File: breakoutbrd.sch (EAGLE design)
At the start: 6 parts

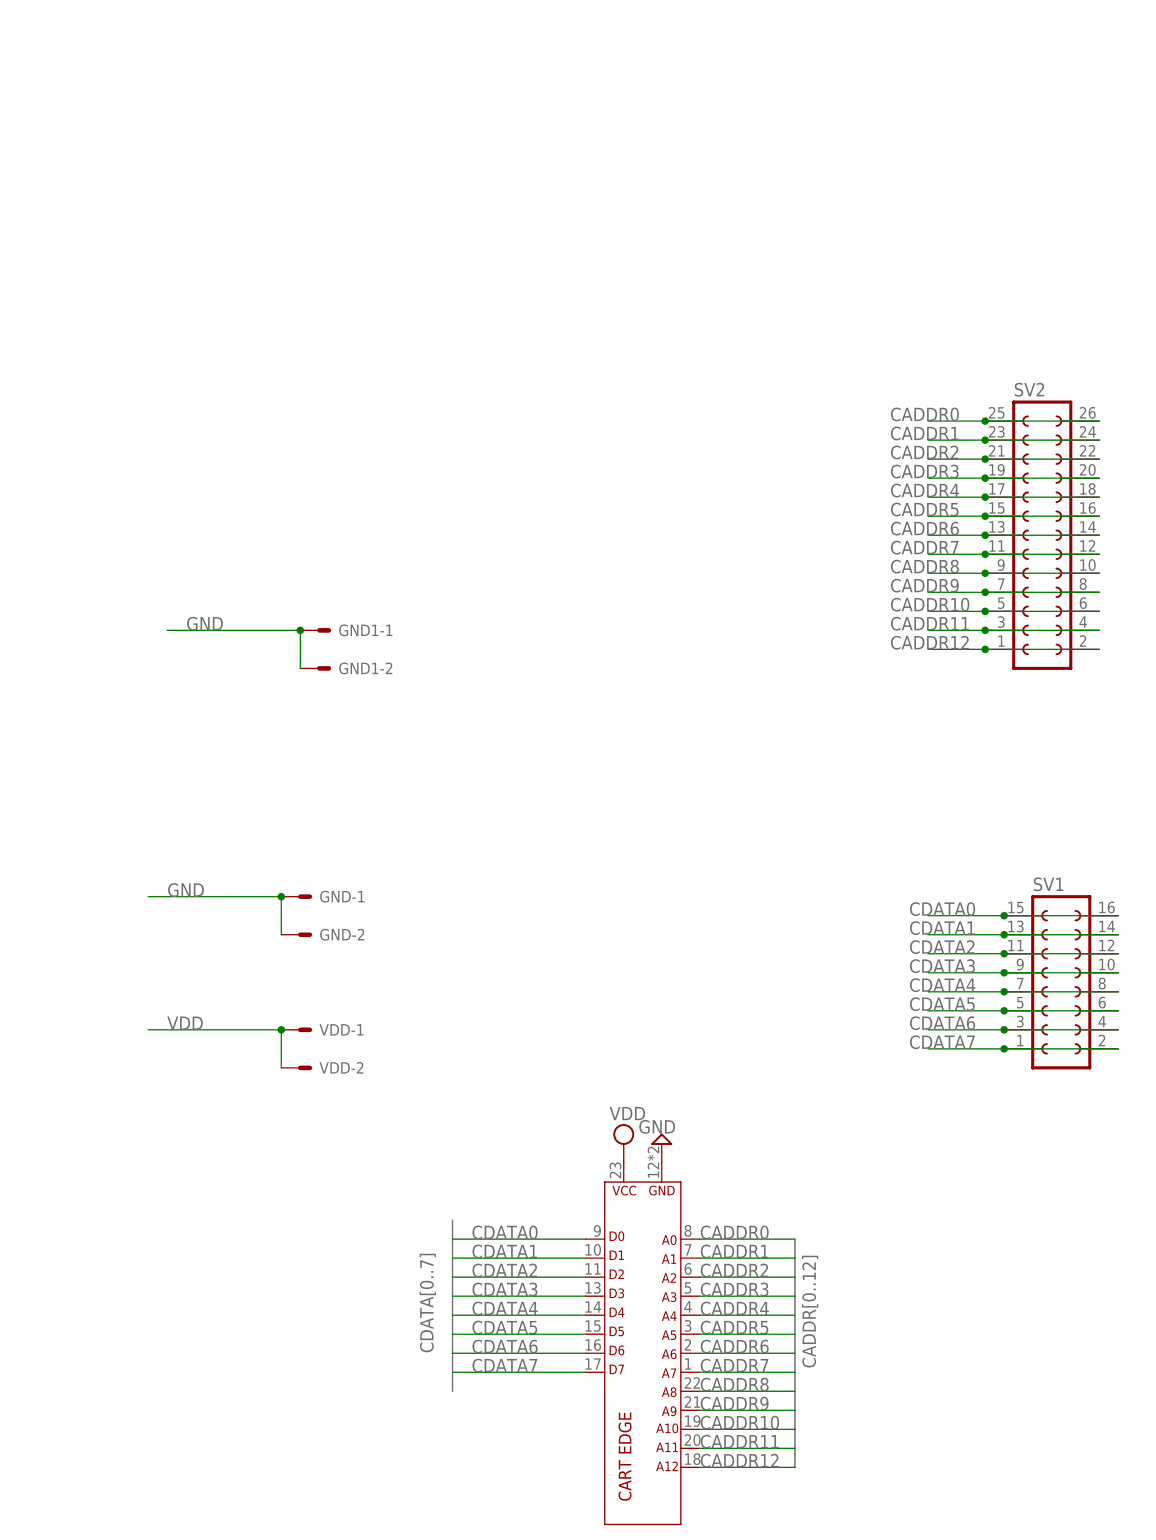
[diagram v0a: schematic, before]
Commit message: optional cartridge connector added to pcb
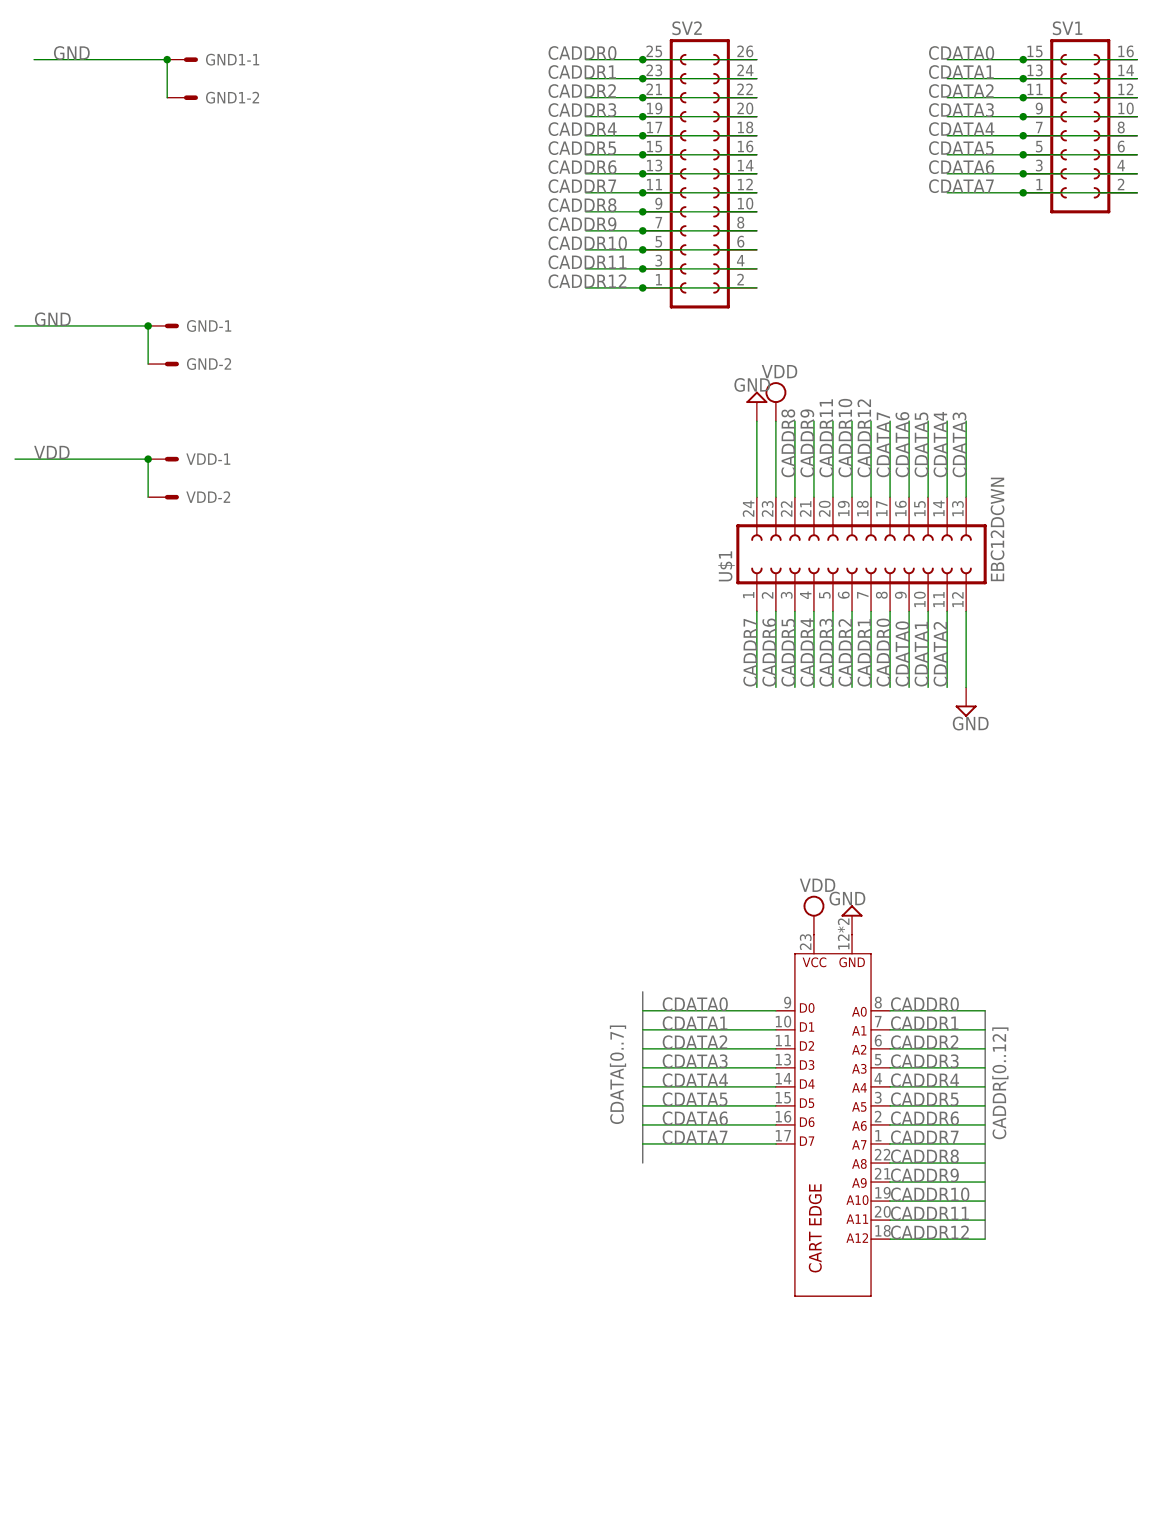
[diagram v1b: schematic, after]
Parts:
- added U$1: EBC12DCWN, a26board:EBC12DCWN
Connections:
- net CADDR0: now also U$1.8
- net CADDR1: now also U$1.7
- net CADDR10: now also U$1.19
- net CADDR11: now also U$1.20
- net CADDR12: now also U$1.18
- net CADDR2: now also U$1.6
- net CADDR3: now also U$1.5
- net CADDR4: now also U$1.4
- net CADDR5: now also U$1.3
- net CADDR6: now also U$1.2
- net CADDR7: now also U$1.1
- net CADDR8: now also U$1.22
- net CADDR9: now also U$1.21
- net CDATA0: now also U$1.9
- net CDATA1: now also U$1.10
- net CDATA2: now also U$1.11
- net CDATA3: now also U$1.13
- net CDATA4: now also U$1.14
- net CDATA5: now also U$1.15
- net CDATA6: now also U$1.16
- net CDATA7: now also U$1.17
- net GND: now also U$1.12, U$1.24
- net VDD: now also U$1.23
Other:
- moved on the sheet: GND-1, GND-2, GND1-1, GND1-2, SV1, SV2, VDD-1, VDD-2

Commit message: working on double sided edge connectors, work in progrss.
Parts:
- J1: device a26board:ATARI-2600MED_NOHOLE -> a26board:ATARI-2600
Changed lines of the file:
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@@
 <grid distance="0.1" unitdist="inch" unit="inch" style="lines" multiple="1" display="no" altdistance="0.02" altunitdist="inch" altunit="inch"/>
 <layers>
-<layer number="1" name="Top" color="4" fill="1" visible="no" active="no"/>
-<layer number="16" name="Bottom" color="1" fill="1" visible="no" active="no"/>
-<layer number="17" name="Pads" color="2" fill="1" visible="no" active="no"/>
-<layer number="18" name="Vias" color="2" fill="1" visible="no" active="no"/>
-<layer number="19" name="Unrouted" color="6" fill="1" visible="no" active="no"/>
-<layer number="20" name="Dimension" color="24" fill="1" visible="no" active="no"/>
-<layer number="21" name="tPlace" color="7" fill="1" visible="no" active="no"/>
-<layer number="22" name="bPlace" color="7" fill="1" visible="no" active="no"/>
-<layer number="23" name="tOrigins" color="15" fill="1" visible="no" active="no"/>
-<layer number="24" name="bOrigins" color="15" fill="1" visible="no" active="no"/>
-<layer number="25" name="tNames" color="7" fill="1" visible="no" active="no"/>
-<layer number="26" name="bNames" color="7" fill="1" visible="no" active="no"/>
-<layer number="27" name="tValues" color="7" fill="1" visible="no" active="no"/>
-<layer number="28" name="bValues" color="7" fill="1" visible="no" active="no"/>
+<layer number="1" name="Top" color="4" fill="1" visible="yes" active="no"/>
+<layer number="16" name="Bottom" color="1" fill="1" visible="yes" active="no"/>
+<layer number="17" name="Pads" color="2" fill="1" visible="yes" active="no"/>
+<layer number="18" name="Vias" color="2" fill="1" visible="yes" active="no"/>
+<layer number="19" name="Unrouted" color="6" fill="1" visible="yes" active="no"/>
+<layer number="20" name="Dimension" color="24" fill="1" visible="yes" active="no"/>
+<layer number="21" name="tPlace" color="7" fill="1" visible="yes" active="no"/>
+<layer number="22" name="bPlace" color="7" fill="1" visible="yes" active="no"/>
+<layer number="23" name="tOrigins" color="15" fill="1" visible="yes" active="no"/>
+<layer number="24" name="bOrigins" color="15" fill="1" visible="yes" active="no"/>
+<layer number="25" name="tNames" color="7" fill="1" visible="yes" active="no"/>
+<layer number="26" name="bNames" color="7" fill="1" visible="yes" active="no"/>
+<layer number="27" name="tValues" color="7" fill="1" visible="yes" active="no"/>
+<layer number="28" name="bValues" color="7" fill="1" visible="yes" active="no"/>
 <layer number="29" name="tStop" color="7" fill="3" visible="no" active="no"/>
 <layer number="30" name="bStop" color="7" fill="6" visible="no" active="no"/>
@@
 <layer number="35" name="tGlue" color="7" fill="4" visible="no" active="no"/>
 <layer number="36" name="bGlue" color="7" fill="5" visible="no" active="no"/>
-<layer number="37" name="tTest" color="7" fill="1" visible="no" active="no"/>
-<layer number="38" name="bTest" color="7" fill="1" visible="no" active="no"/>
+<layer number="37" name="tTest" color="7" fill="1" visible="yes" active="no"/>
+<layer number="38" name="bTest" color="7" fill="1" visible="yes" active="no"/>
 <layer number="39" name="tKeepout" color="4" fill="11" visible="no" active="no"/>
 <layer number="40" name="bKeepout" color="1" fill="11" visible="no" active="no"/>
@@
 <layer number="44" name="Drills" color="7" fill="1" visible="no" active="no"/>
 <layer number="45" name="Holes" color="7" fill="1" visible="no" active="no"/>
-<layer number="46" name="Milling" color="3" fill="1" visible="no" active="no"/>
-<layer number="47" name="Measures" color="7" fill="1" visible="no" active="no"/>
-<layer number="48" name="Document" color="7" fill="1" visible="no" active="no"/>
-<layer number="49" name="Reference" color="7" fill="1" visible="no" active="no"/>
-<layer number="50" name="dxf" color="7" fill="1" visible="no" active="no"/>
-<layer number="51" name="tDocu" color="7" fill="1" visible="no" active="no"/>
-<layer number="52" name="bDocu" color="7" fill="1" visible="no" active="no"/>
-<layer number="53" name="tGND_GNDA" color="7" fill="1" visible="no" active="no"/>
-<layer number="54" name="bGND_GNDA" color="7" fill="1" visible="no" active="no"/>
-<layer number="56" name="wert" color="7" fill="1" visible="no" active="no"/>
-<layer number="57" name="tCAD" color="7" fill="1" visible="no" active="no"/>
-<layer number="59" name="tCarbon" color="7" fill="1" visible="no" active="no"/>
-<layer number="60" name="bCarbon" color="7" fill="1" visible="no" active="no"/>
+<layer number="46" name="Milling" color="3" fill="1" visible="yes" active="no"/>
+<layer number="47" name="Measures" color="7" fill="1" visible="yes" active="no"/>
+<layer number="48" name="Document" color="7" fill="1" visible="yes" active="no"/>
+<layer number="49" name="Reference" color="7" fill="1" visible="yes" active="no"/>
+<layer number="50" name="dxf" color="7" fill="1" visible="yes" active="no"/>
+<layer number="51" name="tDocu" color="7" fill="1" visible="yes" active="no"/>
+<layer number="52" name="bDocu" color="7" fill="1" visible="yes" active="no"/>
+<layer number="53" name="tGND_GNDA" color="7" fill="1" visible="yes" active="no"/>
+<layer number="54" name="bGND_GNDA" color="7" fill="1" visible="yes" active="no"/>
+<layer number="56" name="wert" color="7" fill="1" visible="yes" active="no"/>
+<layer number="57" name="tCAD" color="7" fill="1" visible="yes" active="no"/>
+<layer number="59" name="tCarbon" color="7" fill="1" visible="yes" active="no"/>
+<layer number="60" name="bCarbon" color="7" fill="1" visible="yes" active="no"/>
 <layer number="88" name="SimResults" color="9" fill="1" visible="yes" active="yes"/>
 <layer number="89" name="SimProbes" color="9" fill="1" visible="yes" active="yes"/>
@@
 </classes>
 <parts>
-<part name="J1" library="a26board" deviceset="ATARI-2600" device="MED_NOHOLE"/>
+<part name="J1" library="a26board" deviceset="ATARI-2600" device=""/>
 <part name="SUPPLY10" library="supply2" library_urn="urn:adsk.eagle:library:372" deviceset="VDD" device=""/>
 <part name="SUPPLY11" library="supply2" library_urn="urn:adsk.eagle:library:372" deviceset="GND" device=""/>

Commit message: spread out vias grouped VDD and GND points on same side better labeling
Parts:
- removed GND: 22-23-2021, a26board:22-23-2021
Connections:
- net GND: no longer GND-1.S, GND-2.S
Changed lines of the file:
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@@
 <grid distance="0.1" unitdist="inch" unit="inch" style="lines" multiple="1" display="no" altdistance="0.02" altunitdist="inch" altunit="inch"/>
 <layers>
-<layer number="1" name="Top" color="4" fill="1" visible="yes" active="no"/>
-<layer number="16" name="Bottom" color="1" fill="1" visible="yes" active="no"/>
-<layer number="17" name="Pads" color="2" fill="1" visible="yes" active="no"/>
-<layer number="18" name="Vias" color="2" fill="1" visible="yes" active="no"/>
-<layer number="19" name="Unrouted" color="6" fill="1" visible="yes" active="no"/>
-<layer number="20" name="Dimension" color="24" fill="1" visible="yes" active="no"/>
-<layer number="21" name="tPlace" color="7" fill="1" visible="yes" active="no"/>
-<layer number="22" name="bPlace" color="7" fill="1" visible="yes" active="no"/>
-<layer number="23" name="tOrigins" color="15" fill="1" visible="yes" active="no"/>
-<layer number="24" name="bOrigins" color="15" fill="1" visible="yes" active="no"/>
-<layer number="25" name="tNames" color="7" fill="1" visible="yes" active="no"/>
-<layer number="26" name="bNames" color="7" fill="1" visible="yes" active="no"/>
-<layer number="27" name="tValues" color="7" fill="1" visible="yes" active="no"/>
-<layer number="28" name="bValues" color="7" fill="1" visible="yes" active="no"/>
+<layer number="1" name="Top" color="4" fill="1" visible="no" active="no"/>
+<layer number="16" name="Bottom" color="1" fill="1" visible="no" active="no"/>
+<layer number="17" name="Pads" color="2" fill="1" visible="no" active="no"/>
+<layer number="18" name="Vias" color="2" fill="1" visible="no" active="no"/>
+<layer number="19" name="Unrouted" color="6" fill="1" visible="no" active="no"/>
+<layer number="20" name="Dimension" color="24" fill="1" visible="no" active="no"/>
+<layer number="21" name="tPlace" color="7" fill="1" visible="no" active="no"/>
+<layer number="22" name="bPlace" color="7" fill="1" visible="no" active="no"/>
+<layer number="23" name="tOrigins" color="15" fill="1" visible="no" active="no"/>
+<layer number="24" name="bOrigins" color="15" fill="1" visible="no" active="no"/>
+<layer number="25" name="tNames" color="7" fill="1" visible="no" active="no"/>
+<layer number="26" name="bNames" color="7" fill="1" visible="no" active="no"/>
+<layer number="27" name="tValues" color="7" fill="1" visible="no" active="no"/>
+<layer number="28" name="bValues" color="7" fill="1" visible="no" active="no"/>
 <layer number="29" name="tStop" color="7" fill="3" visible="no" active="no"/>
 <layer number="30" name="bStop" color="7" fill="6" visible="no" active="no"/>
@@
 <layer number="35" name="tGlue" color="7" fill="4" visible="no" active="no"/>
 <layer number="36" name="bGlue" color="7" fill="5" visible="no" active="no"/>
-<layer number="37" name="tTest" color="7" fill="1" visible="yes" active="no"/>
-<layer number="38" name="bTest" color="7" fill="1" visible="yes" active="no"/>
+<layer number="37" name="tTest" color="7" fill="1" visible="no" active="no"/>
+<layer number="38" name="bTest" color="7" fill="1" visible="no" active="no"/>
 <layer number="39" name="tKeepout" color="4" fill="11" visible="no" active="no"/>
 <layer number="40" name="bKeepout" color="1" fill="11" visible="no" active="no"/>
@@
 <layer number="44" name="Drills" color="7" fill="1" visible="no" active="no"/>
 <layer number="45" name="Holes" color="7" fill="1" visible="no" active="no"/>
-<layer number="46" name="Milling" color="3" fill="1" visible="yes" active="no"/>
-<layer number="47" name="Measures" color="7" fill="1" visible="yes" active="no"/>
-<layer number="48" name="Document" color="7" fill="1" visible="yes" active="no"/>
-<layer number="49" name="Reference" color="7" fill="1" visible="yes" active="no"/>
-<layer number="50" name="dxf" color="7" fill="1" visible="yes" active="no"/>
-<layer number="51" name="tDocu" color="7" fill="1" visible="yes" active="no"/>
-<layer number="52" name="bDocu" color="7" fill="1" visible="yes" active="no"/>
-<layer number="53" name="tGND_GNDA" color="7" fill="1" visible="yes" active="no"/>
-<layer number="54" name="bGND_GNDA" color="7" fill="1" visible="yes" active="no"/>
-<layer number="56" name="wert" color="7" fill="1" visible="yes" active="no"/>
-<layer number="57" name="tCAD" color="7" fill="1" visible="yes" active="no"/>
-<layer number="59" name="tCarbon" color="7" fill="1" visible="yes" active="no"/>
-<layer number="60" name="bCarbon" color="7" fill="1" visible="yes" active="no"/>
+<layer number="46" name="Milling" color="3" fill="1" visible="no" active="no"/>
+<layer number="47" name="Measures" color="7" fill="1" visible="no" active="no"/>
+<layer number="48" name="Document" color="7" fill="1" visible="no" active="no"/>
+<layer number="49" name="Reference" color="7" fill="1" visible="no" active="no"/>
+<layer number="50" name="dxf" color="7" fill="1" visible="no" active="no"/>
+<layer number="51" name="tDocu" color="7" fill="1" visible="no" active="no"/>
+<layer number="52" name="bDocu" color="7" fill="1" visible="no" active="no"/>
+<layer number="53" name="tGND_GNDA" color="7" fill="1" visible="no" active="no"/>
+<layer number="54" name="bGND_GNDA" color="7" fill="1" visible="no" active="no"/>
+<layer number="56" name="wert" color="7" fill="1" visible="no" active="no"/>
+<layer number="57" name="tCAD" color="7" fill="1" visible="no" active="no"/>
+<layer number="59" name="tCarbon" color="7" fill="1" visible="no" active="no"/>
+<layer number="60" name="bCarbon" color="7" fill="1" visible="no" active="no"/>
 <layer number="88" name="SimResults" color="9" fill="1" visible="yes" active="yes"/>
 <layer number="89" name="SimProbes" color="9" fill="1" visible="yes" active="yes"/>
@@
 <part name="SV1" library="a26board" deviceset="FE08-2" device="" package3d_urn="urn:adsk.eagle:package:8174/1"/>
 <part name="SV2" library="a26board" deviceset="FE13-2" device="" package3d_urn="urn:adsk.eagle:package:8172/1"/>
-<part name="GND" library="a26board" deviceset="22-23-2021" device="" package3d_urn="urn:adsk.eagle:package:8078633/1"/>
 <part name="VDD" library="a26board" deviceset="22-23-2021" device="" package3d_urn="urn:adsk.eagle:package:8078633/1"/>
 <part name="GND1" library="a26board" deviceset="22-23-2021" device="" package3d_urn="urn:adsk.eagle:package:8078633/1"/>
@@
 <attribute name="NAME" x="95.25" y="211.582" size="1.778" layer="95"/>
 </instance>
-<instance part="GND" gate="-1" x="27.94" y="172.72" smashed="yes">
-<attribute name="NAME" x="30.48" y="171.958" size="1.524" layer="95"/>
-</instance>
-<instance part="GND" gate="-2" x="27.94" y="167.64" smashed="yes">
-<attribute name="NAME" x="30.48" y="166.878" size="1.524" layer="95"/>
-</instance>
 <instance part="VDD" gate="-1" x="27.94" y="154.94" smashed="yes">
 <attribute name="NAME" x="30.48" y="154.178" size="1.524" layer="95"/>
@@
 </segment>
 <segment>
-<pinref part="GND" gate="-1" pin="S"/>
-<wire x1="25.4" y1="172.72" x2="7.62" y2="172.72" width="0.1524" layer="91"/>
-<pinref part="GND" gate="-2" pin="S"/>
-<wire x1="25.4" y1="167.64" x2="25.4" y2="172.72" width="0.1524" layer="91"/>
-<junction x="25.4" y="172.72"/>
-<label x="10.16" y="172.72" size="1.778" layer="95"/>
-</segment>
-<segment>
